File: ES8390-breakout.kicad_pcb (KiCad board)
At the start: 2 copper layers, 36 parts, among them CN1 PJ-327A, CN2 PJ-327A, J1 Conn_01x02_Pin, J2 Conn_01x02_Pin, J3 AV-5, J4 AV-5, J5 Conn_01x14_Pin, U1 LP5907MFX-3.0, U2 MAX98306xDT, U3 ES8390, U4 IM68A130AXTMA1, U5 IM68A130AXTMA1

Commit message: guitar input stage?
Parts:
- added H1: MountingHole, MountingHole:MountingHole_3.2mm_M3_DIN965, F.Cu at (146.5, 23.5)
- added H2: MountingHole, MountingHole:MountingHole_3.2mm_M3_DIN965, F.Cu at (146.5, 86.5)
- added H3: MountingHole, MountingHole:MountingHole_3.2mm_M3_DIN965, F.Cu at (116.1, 143.4)
- added H4: MountingHole, MountingHole:MountingHole_3.2mm_M3_DIN965, F.Cu at (116.1, 150.5)
- C13, C14, C7: value 1u -> 100n
- moved C14 90.2 mm to (51.8, 162.0)
- moved C1 85.1 mm to (-15.8, 113.5)
- moved C10 85.1 mm to (-9.79, 113.5)
- moved C11 85.1 mm to (-9.68, 149.9)
- moved C12 85.1 mm to (-9.68, 152.4)
- moved C15 85.1 mm to (-5.67, 144.9)
- moved C16 85.1 mm to (-5.67, 147.4)
- moved C17 85.1 mm to (-5.67, 149.9)
- moved C18 85.1 mm to (-5.67, 152.4)
- moved C19 85.1 mm to (-1.66, 139.9)
- moved C2 85.1 mm to (-13.7, 142.4)
- moved C20 85.1 mm to (-1.66, 142.4)
- moved C3 85.1 mm to (-13.7, 144.9)
- moved C4 85.1 mm to (80.2, 131.0)
- moved C5 85.1 mm to (-13.7, 149.9)
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- renumbered J3 to CN1, J4 to CN2, J5 to CN3, CN1 to CN4, CN2 to CN5
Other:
- board outline added: 50 x 70 mm

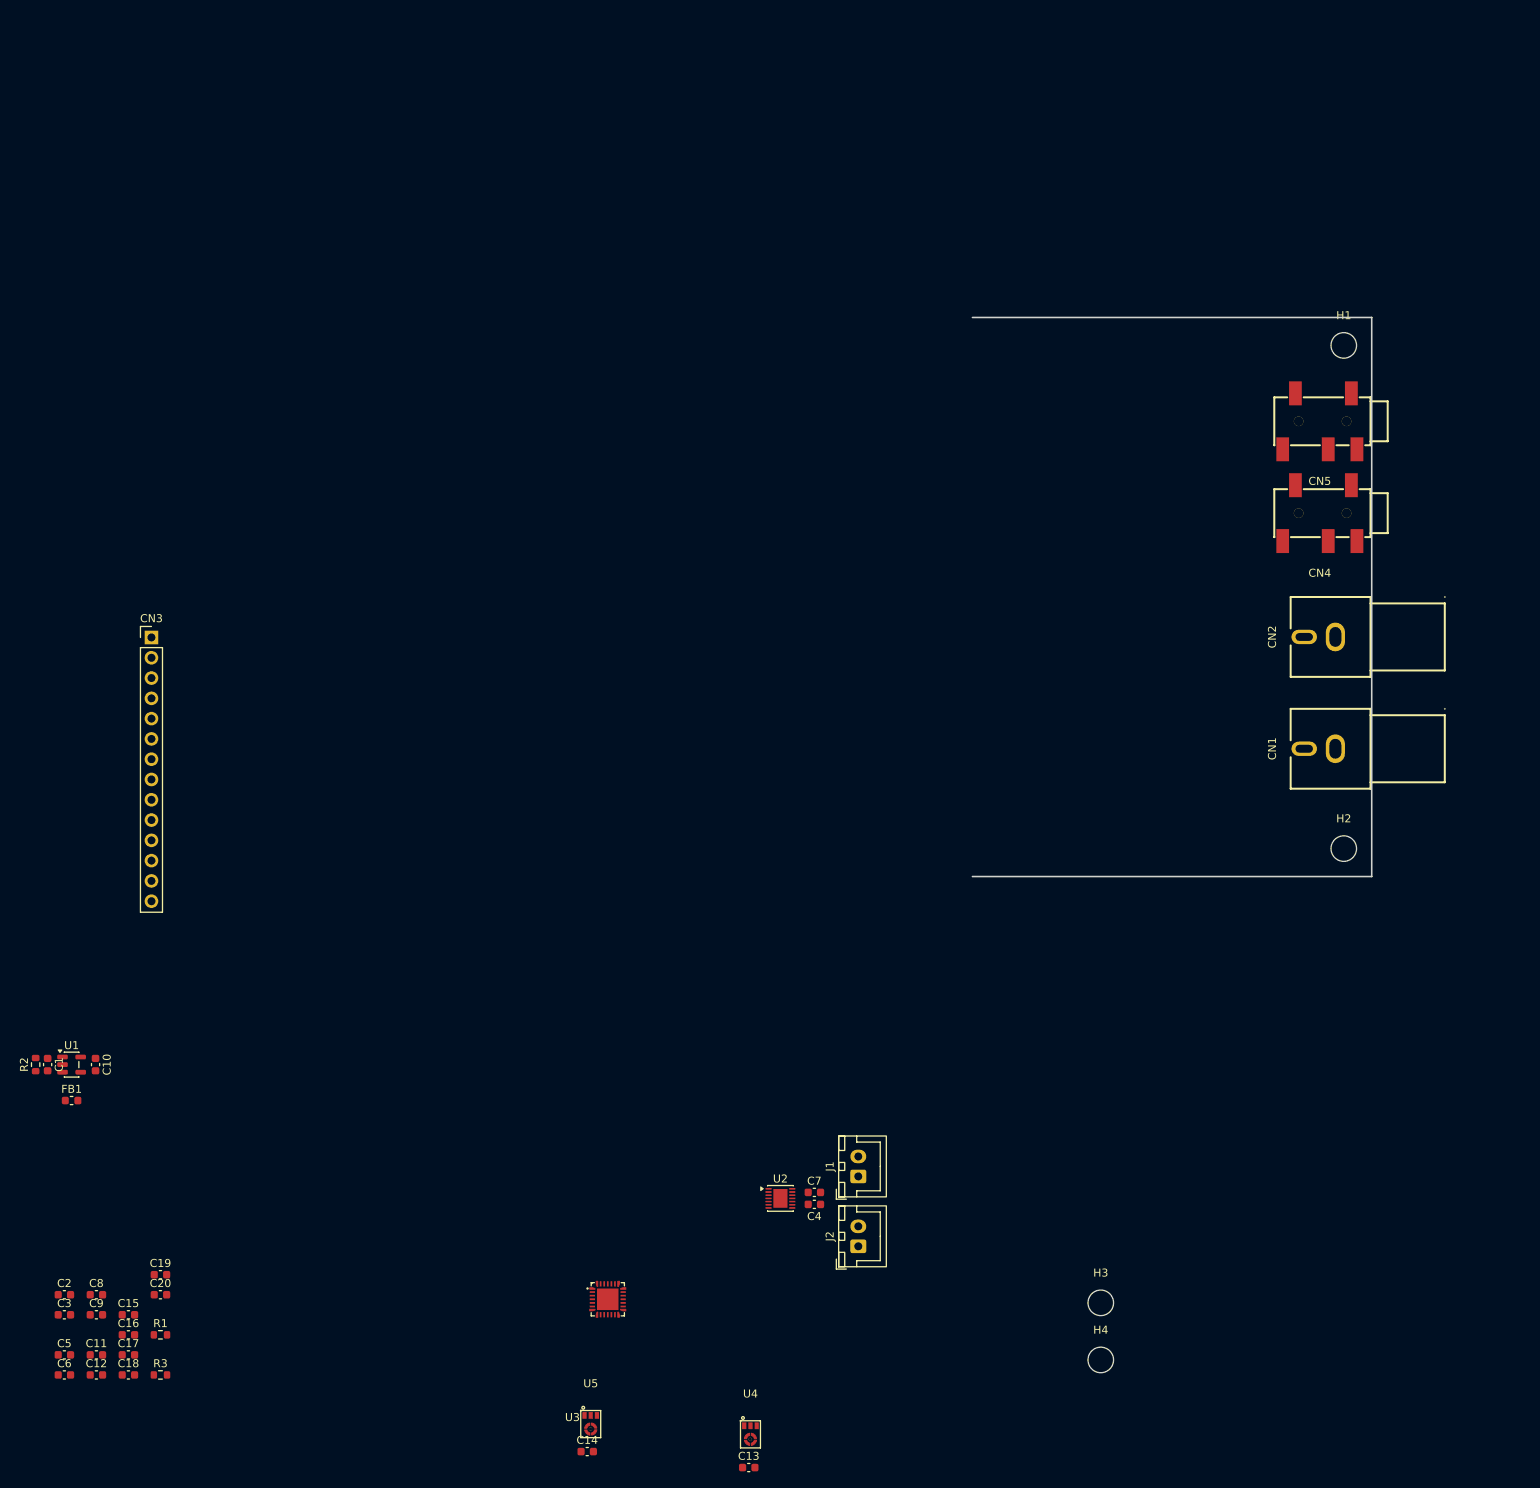
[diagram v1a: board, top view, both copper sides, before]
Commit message: add lcsc parts, ts-mono jack
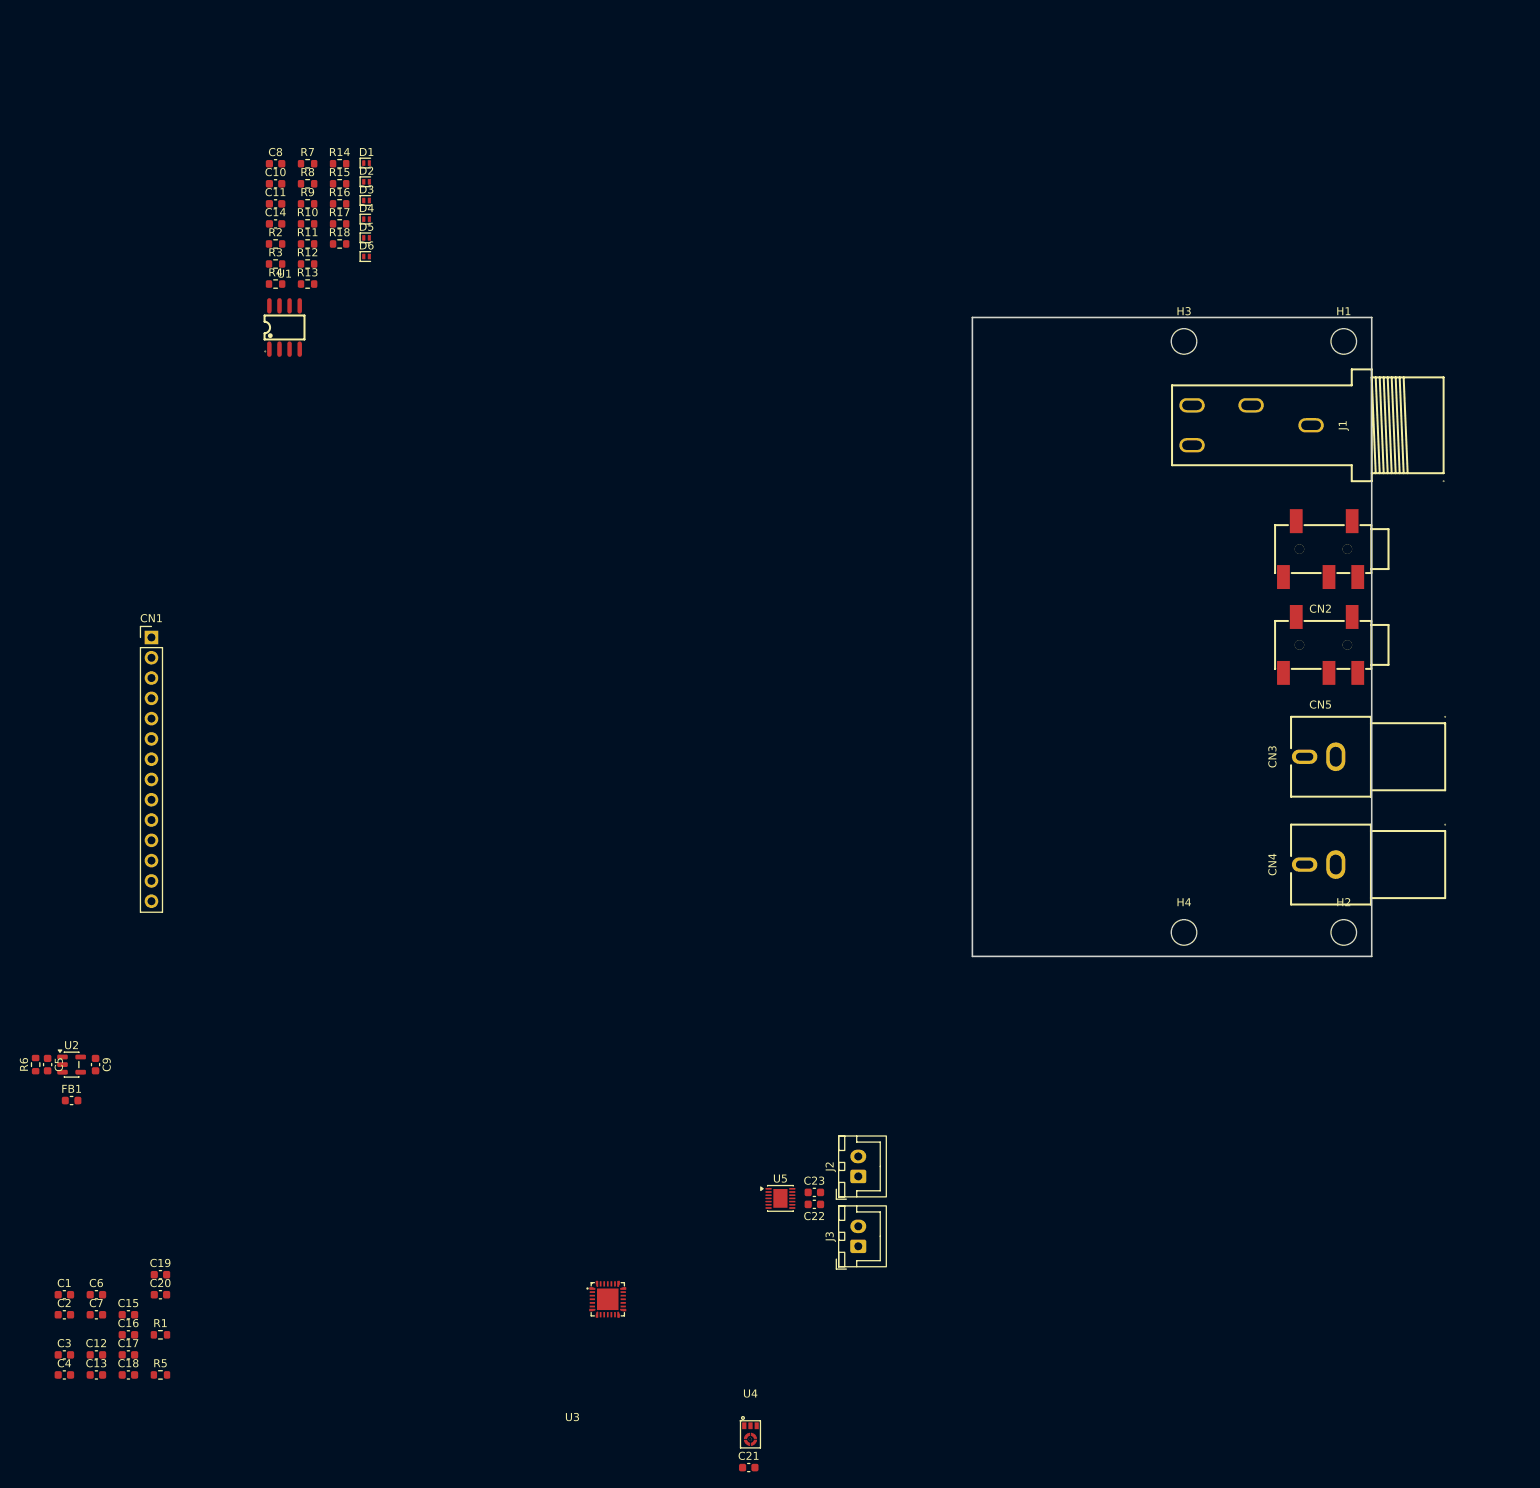
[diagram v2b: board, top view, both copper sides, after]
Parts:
- removed the CN1 at (143.5, 74.0)
- removed the U5 at (52.2, 158.5)
- added C10: 100n, Capacitor_SMD:C_0603_1608Metric, F.Cu at (12.8, 3.27)
- added C11: 100p, Capacitor_SMD:C_0603_1608Metric, F.Cu at (12.8, 5.78)
- added C8: 100p, Capacitor_SMD:C_0603_1608Metric, F.Cu at (12.8, 0.76)
- added CN4: AV-5, lcsc:CONN-TH_AV-5, F.Cu at (143.6, 88.5)
- added D1: UAD8C05L01-ES, Diode_SMD:D_SOD-882, F.Cu at (24.1, 0.67)
- added D2: UAD8C05L01-ES, Diode_SMD:D_SOD-882, F.Cu at (24.1, 3.01)
- added D3: UAD8C05L01-ES, Diode_SMD:D_SOD-882, F.Cu at (24.1, 5.35)
- added D4: UAD8C05L01-ES, Diode_SMD:D_SOD-882, F.Cu at (24.1, 7.69)
- added D5: UAD8C05L01-ES, Diode_SMD:D_SOD-882, F.Cu at (24.1, 10.0)
- added D6: UAD8C05L01-ES, Diode_SMD:D_SOD-882, F.Cu at (24.1, 12.4)
- added J1: PJ-603A, lcsc:AUDIO-TH_PJ-603A, F.Cu at (134.9, 33.5)
- added R10: 1M, Resistor_SMD:R_0603_1608Metric, F.Cu at (16.8, 8.29)
- added R11: 4k7, Resistor_SMD:R_0603_1608Metric, F.Cu at (16.8, 10.8)
- added R12: 10k, Resistor_SMD:R_0603_1608Metric, F.Cu at (16.8, 13.3)
- added R13: 10k, Resistor_SMD:R_0603_1608Metric, F.Cu at (16.8, 15.8)
- added R14: 4R7, Resistor_SMD:R_0603_1608Metric, F.Cu at (20.8, 0.76)
- added R15: 100R, Resistor_SMD:R_0603_1608Metric, F.Cu at (20.8, 3.27)
- added R16: 100R, Resistor_SMD:R_0603_1608Metric, F.Cu at (20.8, 5.78)
- added R17: 4k7, Resistor_SMD:R_0603_1608Metric, F.Cu at (20.8, 8.29)
- added R18: 4k7, Resistor_SMD:R_0603_1608Metric, F.Cu at (20.8, 10.8)
- added R2: 100k, Resistor_SMD:R_0603_1608Metric, F.Cu at (12.8, 10.8)
- added R3: 100k, Resistor_SMD:R_0603_1608Metric, F.Cu at (12.8, 13.3)
- added R4: 4R7, Resistor_SMD:R_0603_1608Metric, F.Cu at (12.8, 15.8)
- added R7: 0, Resistor_SMD:R_0603_1608Metric, F.Cu at (16.8, 0.76)
- added R8: 0, Resistor_SMD:R_0603_1608Metric, F.Cu at (16.8, 3.27)
- added R9: 1M, Resistor_SMD:R_0603_1608Metric, F.Cu at (16.8, 5.78)
- added U1: TLV9062, lcsc:SOIC-8_L5.0-W4.0-P1.27-LS6.0-BL, F.Cu at (13.9, 21.3)
- moved C14 158.6 mm to (12.8, 8.29)
- moved H3 120.8 mm to (126.5, 23.0)
- moved H4 54.5 mm to (126.5, 97.0)
- moved CN5 16.5 mm to (143.6, 61.0)
- moved CN2 16.0 mm to (143.6, 49.0)
- moved CN3 15.0 mm to (143.6, 75.0)
- moved H2 10.5 mm to (146.5, 97.0)
- moved H1 0.50 mm to (146.5, 23.0)
- renumbered C2 to C1, C11 to C12, C12 to C13, C3 to C2, C13 to C21, C4 to C22, C7 to C23, C5 to C3, C6 to C4, C1 to C5, C8 to C6, C9 to C7, C10 to C9, CN3 to CN1, CN5 to CN2, CN2 to CN3, CN4 to CN5, J1 to J2, J2 to J3, R3 to R5, R2 to R6, U1 to U2, U2 to U5
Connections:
- C12 pad 1: LOUTP -> Net-(C12-Pad1)
- C16 pad 2: LIN1 -> Net-(C16-Pad2)
- C18 pad 2: RIN1 -> Net-(C18-Pad2)
- C19 pad 1: RIN2 -> Net-(C19-Pad1)
- C20 pad 2: LIN2 -> Net-(C20-Pad2)
- C3 pad 1: ROUTP -> Net-(C3-Pad1)
- C6 pad 1: LOUTN -> Net-(C6-Pad1)
- C7 pad 1: ROUTN -> Net-(C7-Pad1)
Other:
- board size 50 x 70 mm -> 50 x 80 mm

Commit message: continue layout
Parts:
- moved C21 152.3 mm to (129.5, 23.0), turned to -90 degrees
- moved U4 148.6 mm to (132.5, 24.0), turned to 90 degrees
- moved CN1 114.1 mm to (111.0, 68.2), turned to 180 degrees
- moved U5 82.7 mm to (128.2, 66.2), turned to -90 degrees
- moved C22 76.8 mm to (127.5, 70.5), turned to -90 degrees
- moved C23 76.6 mm to (129.0, 70.5), turned to -90 degrees
- moved J3 70.5 mm to (122.2, 76.0), turned to 0 degrees
- moved J2 68.6 mm to (131.0, 76.0), turned to 0 degrees
- moved U1 50.6 mm to (52.5, -11.5), turned to -90 degrees
- moved R3 49.0 mm to (52.0, -16.0), turned to 90 degrees
- moved R2 48.8 mm to (53.5, -16.0), turned to -90 degrees
- moved C14 48.7 mm to (55.0, -16.0), turned to 90 degrees
- moved R12 42.8 mm to (56.5, -2.50)
- moved R13 42.8 mm to (56.5, 0.01)
- moved C8 41.3 mm to (50.5, -16.0), turned to 90 degrees
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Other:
- board size 50 x 80 mm -> 41 x 60 mm

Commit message: continue layout
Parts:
- removed the CN3 at (141.0, 103.0)
- removed CN4: AV-5, lcsc:CONN-TH_AV-5
- removed the D1 at (24.1, 0.67)
- removed the D4 at (24.1, 7.69)
- added C21: 1u, Capacitor_SMD:C_0603_1608Metric, F.Cu at (93.8, 97.6)
- added C22: 1u, Capacitor_SMD:C_0603_1608Metric, F.Cu at (92.3, 97.6)
- added R19: 0, Resistor_SMD:R_0603_1608Metric, F.Cu at (96.2, 103.2)
- added R20: 0, Resistor_SMD:R_0603_1608Metric, F.Cu at (97.8, 103.2)
- U3: footprint lcsc:QFN-28_L4.0-W4.0-P0.45-TL-EP2.7 -> Package_DFN_QFN:QFN-28-1EP_4x4mm_P0.45mm_EP2.6x2.6mm
- moved C18 143.9 mm to (106.8, 62.5)
- moved C4 137.7 mm to (104.1, 81.0), turned to 90 degrees
- moved C16 135.7 mm to (100.2, 62.5), turned to 180 degrees
- moved C1 134.1 mm to (105.6, 81.0), turned to 90 degrees
- moved R14 130.9 mm to (108.4, 98.0)
- moved C13 130.4 mm to (105.1, 90.5), turned to -90 degrees
- moved C20 130.2 mm to (114.2, 83.0)
- moved C19 129.7 mm to (114.2, 81.5), turned to 180 degrees
- moved C3 129.3 mm to (105.4, 99.5), turned to 180 degrees
- moved C2 128.5 mm to (100.0, 85.0), turned to 180 degrees
- moved R1 127.4 mm to (107.1, 81.0), turned to 90 degrees
- moved R4 127.1 mm to (108.4, 99.5)
- moved R5 126.4 mm to (102.6, 81.0), turned to 90 degrees
- moved C12 126.2 mm to (105.4, 98.0), turned to 180 degrees
- moved C15 124.7 mm to (106.6, 90.5), turned to -90 degrees
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- renumbered C22 to C23, C23 to C24, C21 to C25, CN5 to CN3, D2 to D1, D3 to D2, D5 to D3, D6 to D4
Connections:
- CN1 pad 1: VAMP -> GND
- CN1 pad 2: VLDO -> VAMP
- CN1 pad 3: GND -> VLDO
- CN1 pad 5: GND -> AMP_SHDN
- R13 pad 2: RIN1 -> LIN1
- U1 pad 7: RIN1 -> LIN1
- U3 pad 26: unconnected-(U3-AD0/DMIC_SCL-Pad26) -> AD0/DMIC_SCL
- U3 pad 27: unconnected-(U3-CDATA-Pad27) -> CDATA
- U3 pad 28: unconnected-(U3-CCLK-Pad28) -> CCLK
- U4 pad 1: LIN1 -> RIN1
- U5 pad 2: unconnected-(U5-~{SHDN}-Pad2) -> AMP_SHDN
- U5 pad 4: unconnected-(U5-INL--Pad4) -> Net-(U5-INL-)
- U5 pad 5: unconnected-(U5-GAIN-Pad5) -> Net-(U5-GAIN)
- U5 pad 6: unconnected-(U5-INR--Pad6) -> Net-(U5-INR-)
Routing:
- net VDDA: track 0.00 -> 62.8 mm
- net Net-(U3-LIN1/DMIC_SDA): track 0.00 -> 30.8 mm
- net Net-(U3-RIN1/DMIC_SCL): track 0.00 -> 29.2 mm
- net VAMP: track 0.00 -> 25.2 mm, vias 0 -> 2
- net GND: track 0.00 -> 19.5 mm, vias 0 -> 52
- net RIN2: track 0.00 -> 18.4 mm
- net Net-(U3-ROUTP): track 0.00 -> 17.5 mm, vias 0 -> 2
- net Net-(J2-Pin_1): track 0.00 -> 15.9 mm
- net Net-(U3-ROUTN): track 0.00 -> 14.9 mm
- net ROUTP: track 0.00 -> 14.7 mm
- net Net-(J2-Pin_2): track 0.00 -> 13.9 mm
- net VIO: track 0.00 -> 13.6 mm
- net Net-(U3-LOUTN): track 0.00 -> 13.0 mm, vias 0 -> 2
- net Net-(J3-Pin_1): track 0.00 -> 12.8 mm, vias 0 -> 2
- net AMP_SHDN: track 0.00 -> 12.7 mm, vias 0 -> 2
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- added copper zone on F.Cu, net GND
- added copper zone on In1.Cu, net GND
- added copper zone on In2.Cu, net GND
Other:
- board size 41 x 60 mm -> 40.5 x 60 mm
- copper layers 2 -> 4

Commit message: first layout done
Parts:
- moved C5 16.5 mm to (105.5, 79.2)
- moved R6 16.0 mm to (107.0, 79.2), turned to -90 degrees
- moved R1 15.6 mm to (92.1, 85.5), turned to 180 degrees
- moved C1 14.8 mm to (92.1, 87.0), turned to 180 degrees
- moved C4 14.1 mm to (92.1, 88.5), turned to 180 degrees
- moved R5 13.8 mm to (92.1, 90.0), turned to 180 degrees
- moved C9 12.2 mm to (102.2, 81.5), turned to 0 degrees
- moved U2 11.0 mm to (102.7, 78.8), turned to 180 degrees
- moved C2 9.10 mm to (95.8, 93.0), turned to -90 degrees
- moved U3 8.12 mm to (97.2, 88.2), turned to 0 degrees
- moved C21 7.85 mm to (100.0, 102.5)
- moved C22 7.85 mm to (98.5, 102.5)
- moved C6 7.85 mm to (101.5, 99.5)
- moved C7 7.85 mm to (97.0, 99.5)
- moved R7 7.85 mm to (101.5, 102.5)
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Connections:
- CN1 pad 10: ADOUT/AD1 -> MCLK
- CN1 pad 11: CDATA -> CCLK
- CN1 pad 12: CCLK -> CDATA
- CN1 pad 6: MCLK -> ADOUT/AD1
- CN1 pad 7: SCLK -> LRCK
- CN1 pad 8: LRCK -> DSDIN
- CN1 pad 9: DSDIN -> SCLK
- U3 pad 1: unconnected-(U3-MCLK/DMIC_SCL/TDMIN-Pad1) -> MCLK
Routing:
- net VLDO: track 3.68 -> 41.0 mm, vias 0 -> 3
- net AMP_SHDN: track 12.7 -> 31.2 mm
- net AD0/DMIC_SCL: track 0.00 -> 16.9 mm, vias 0 -> 1
- net VDDA: track 62.8 -> 78.5 mm, vias 0 -> 2
- net CDATA: track 0.00 -> 15.1 mm, vias 0 -> 1
- net CCLK: track 0.00 -> 13.3 mm, vias 0 -> 1
- net ADOUT/AD1: track 0.00 -> 12.0 mm, vias 0 -> 1
- net MCLK: track 0.00 -> 11.9 mm, vias 0 -> 1
- net SCLK: track 0.00 -> 11.6 mm, vias 0 -> 1
- net DSDIN: track 0.00 -> 11.3 mm, vias 0 -> 1
- net VIO: track 13.6 -> 24.6 mm
- net Net-(U5-GAIN): track 0.00 -> 10.8 mm, vias 0 -> 2
- net LRCK: track 0.00 -> 10.6 mm, vias 0 -> 1
- net VAMP: track 25.2 -> 17.2 mm, vias 2 -> 0
- net Net-(U3-LIN2): track 9.01 -> 16.2 mm
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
